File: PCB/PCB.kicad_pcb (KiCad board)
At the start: 2 copper layers, 1 part, among them U1 ESP32-DEVKIT-V1

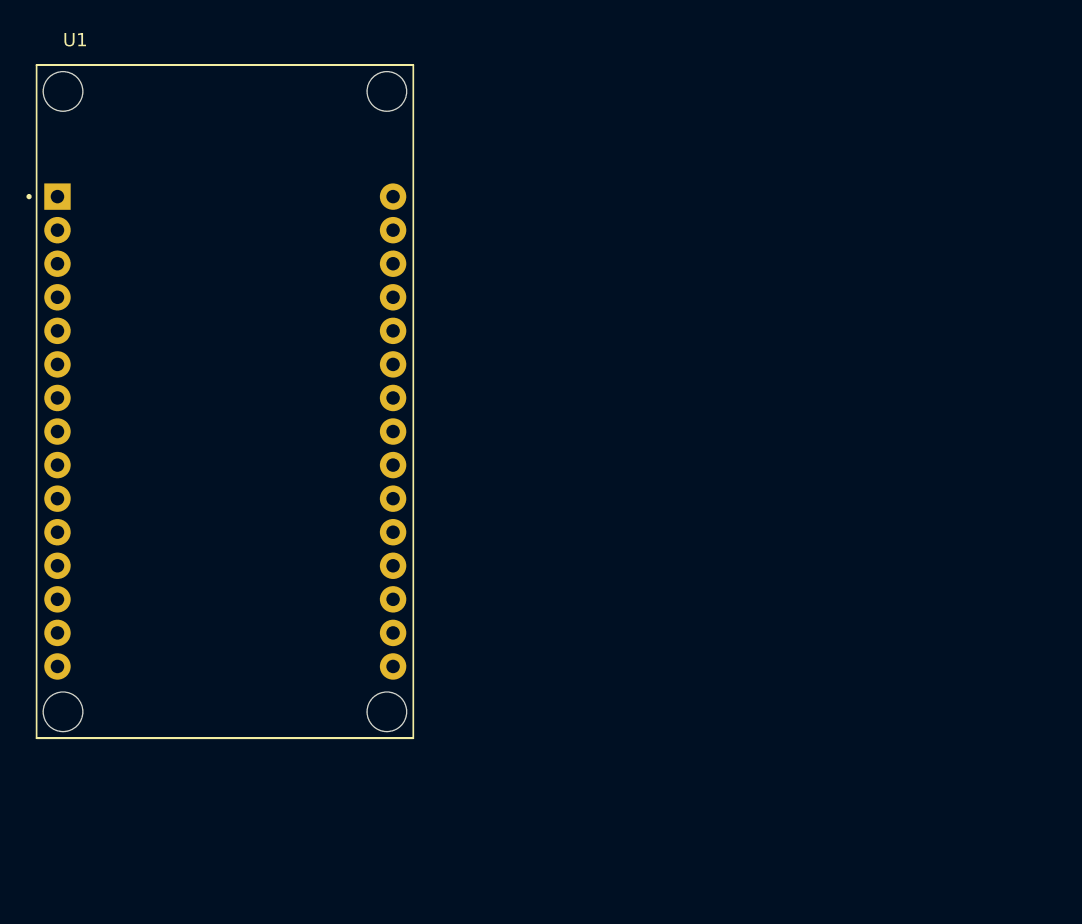
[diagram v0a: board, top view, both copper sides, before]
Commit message: Correccion agujeros PCB
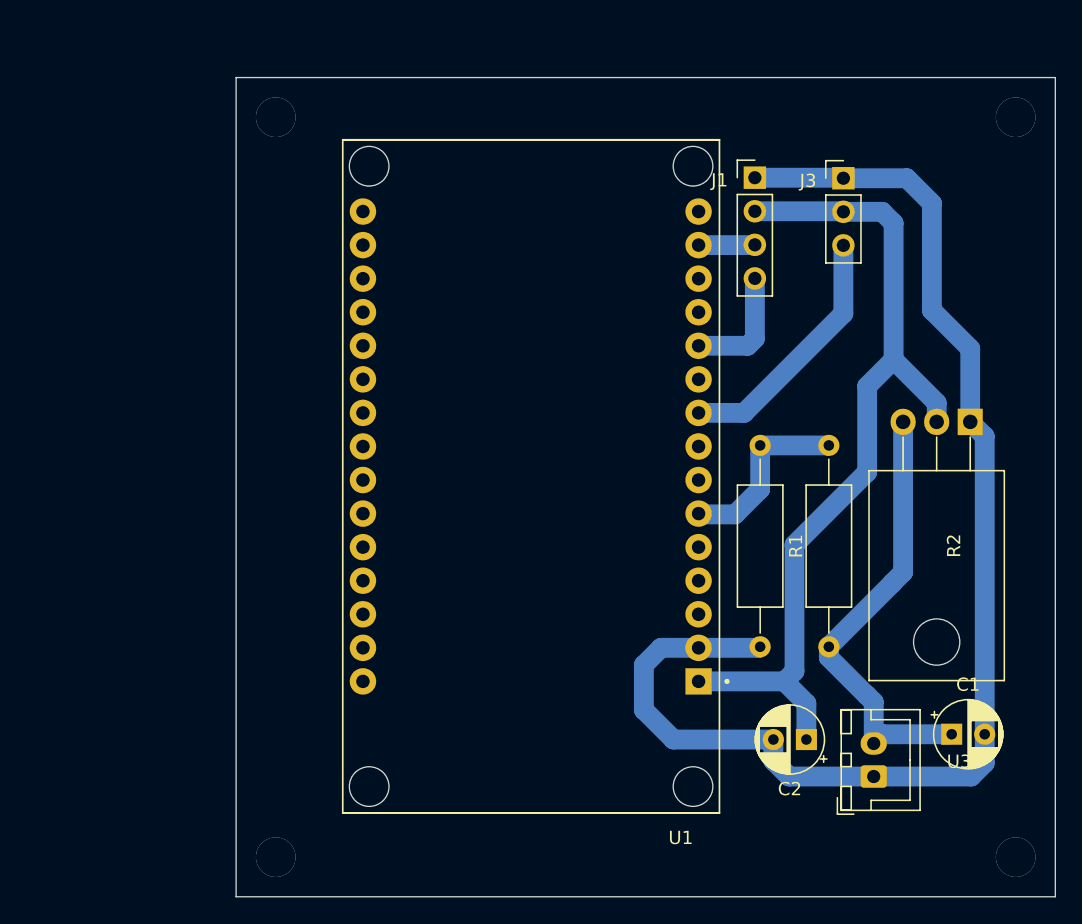
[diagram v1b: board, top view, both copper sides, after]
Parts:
- added C1: C, Capacitor_THT:CP_Radial_D5.0mm_P2.50mm, F.Cu at (223.2, 88.7)
- added C2: C, Capacitor_THT:CP_Radial_D5.0mm_P2.50mm, F.Cu at (212.2, 89.1)
- added J1: OLED, Connector_PinHeader_2.54mm:PinHeader_1x04_P2.54mm_Vertical, F.Cu at (208.3, 46.6)
- added J2: BATT, Connector_JST:JST_XH_B2B-XH-A_1x02_P2.50mm_Vertical, F.Cu at (217.3, 91.9)
- added J3: DHT11, Connector_PinHeader_2.54mm:PinHeader_1x03_P2.54mm_Vertical, F.Cu at (215.0, 46.6)
- added R1: R, Resistor_THT:R_Axial_DIN0309_L9.0mm_D3.2mm_P15.24mm_Horizontal, F.Cu at (208.7, 66.8)
- added R2: R, Resistor_THT:R_Axial_DIN0309_L9.0mm_D3.2mm_P15.24mm_Horizontal, F.Cu at (213.9, 82.1)
- added U3: LM1117T-3.3, Package_TO_SOT_THT:TO-220-3_Horizontal_TabDown, F.Cu at (224.6, 65.1)
- moved U1 23.8 mm to (191.3, 69.2), turned to 180 degrees
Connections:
- net Net-(U1-GND-Pad2) renamed GND
- U1 pad 1: unconnected-(U1-3V3-Pad1) -> +3.3V
- U1 pad 11: unconnected-(U1-D21-Pad11) -> SDA
- U1 pad 14: unconnected-(U1-D22-Pad14) -> SCL
- U1 pad 6: unconnected-(U1-RX2-Pad6) -> ADC_BATT
- U1 pad 9: unconnected-(U1-D18-Pad9) -> DATA_DHT11
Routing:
- net GND: track 0.00 -> 100.2 mm
- net +3.3V: track 0.00 -> 66.6 mm
- net BATT+: track 0.00 -> 34.3 mm
- net DATA_DHT11: track 0.00 -> 19.2 mm
- net ADC_BATT: track 0.00 -> 14.0 mm
- net SDA: track 0.00 -> 9.10 mm
- net SCL: track 0.00 -> 4.27 mm
- net (no net): vias 0 -> 4
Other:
- board outline added: 62 x 62 mm
